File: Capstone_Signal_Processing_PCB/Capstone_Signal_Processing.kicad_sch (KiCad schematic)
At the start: 21 parts, among them J1 Conn_01x01, J2 Conn_01x01, J3 Conn_01x01, J4 Conn_01x04, J5 Conn_01x02, U1 AD4170-4BCPZ

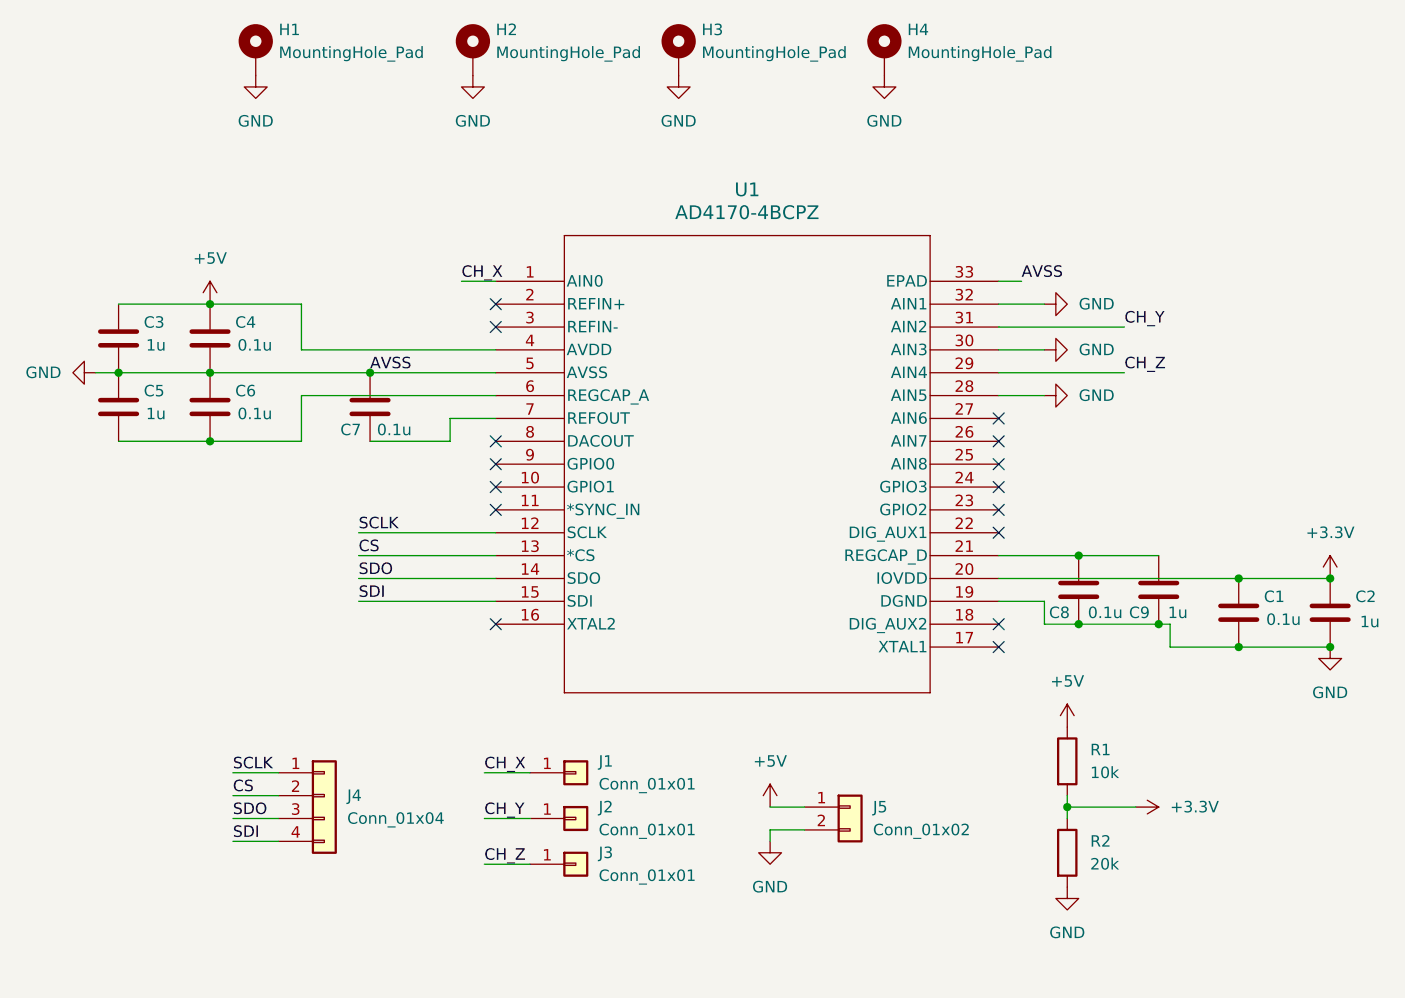
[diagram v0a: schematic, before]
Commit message: Fixes to Signal Processing PCB, Tx-Rx Added
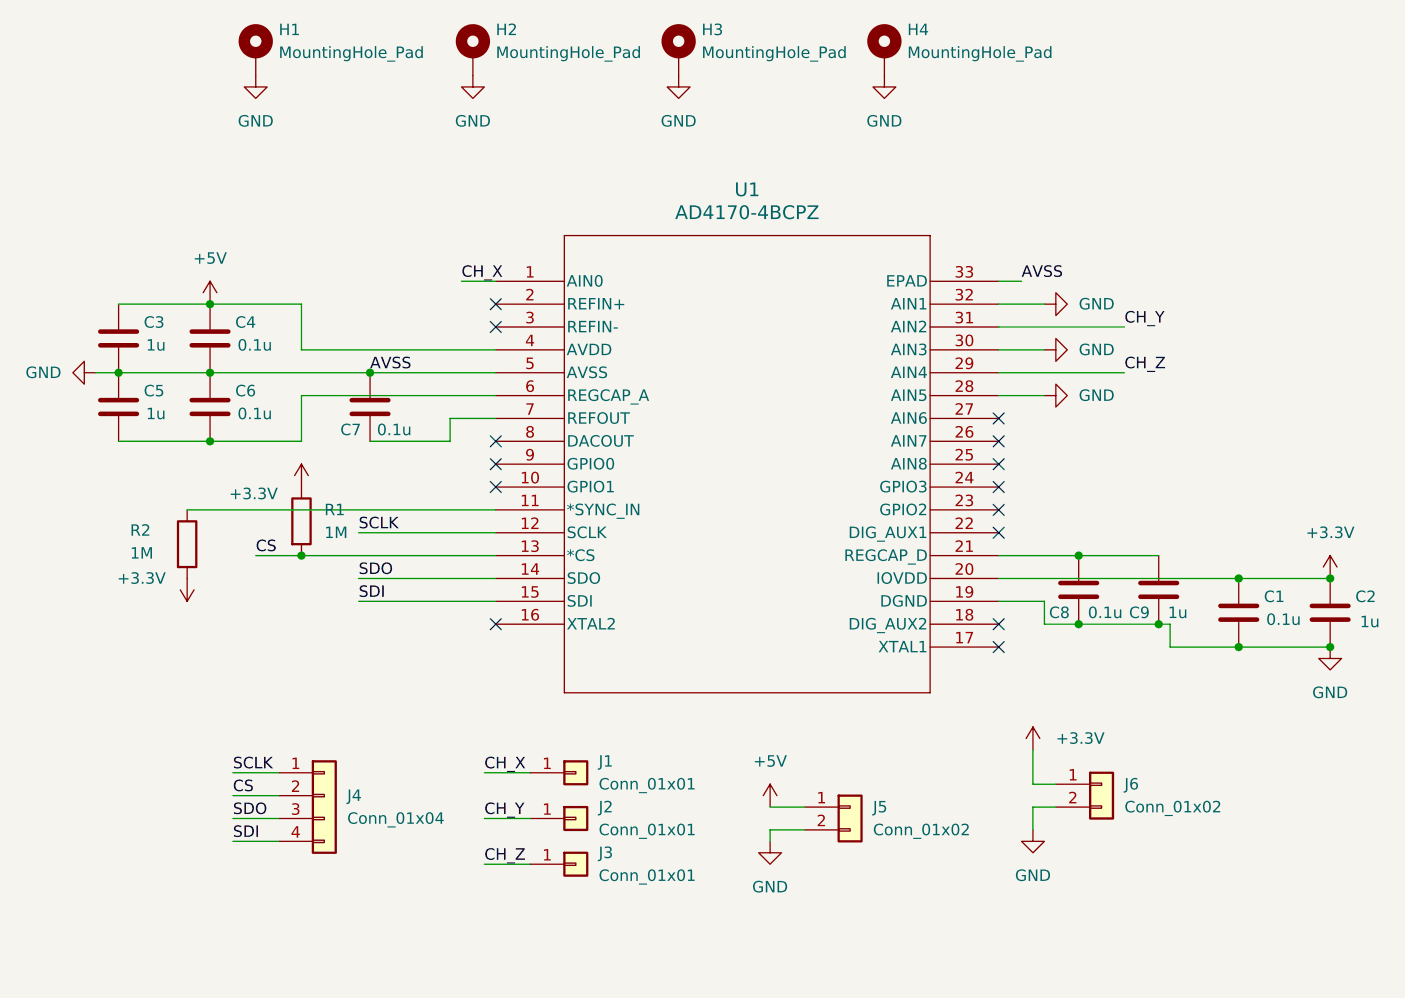
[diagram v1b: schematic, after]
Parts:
- added J6: Conn_01x02, Connector_JST:JST_XH_B2B-XH-AM_1x02_P2.50mm_Vertical, symbol Connector_Generic:Conn_01x02
- R1: value 10k -> 1M
- R2: value 20k -> 1M
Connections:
- net +3.3V: now also R1.1, R2.2, J6.1 (Pin_1); no longer R1.2, R2.1
- net +5V: no longer R1.1
- net CS: now also R1.2
- net GND: now also J6.2 (Pin_2); no longer R2.2
- net at U1.11 (*SYNC_IN): now also R2.1
- no-connect marks 15 -> 14

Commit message: Final Changes to ADC PCB
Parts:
- removed J1, J2, J3: Conn_01x01, Connector_JST:JST_XH_B1B-XH-AM_1x01_P2.50mm_Vertical, symbol Connector_Generic:Conn_01x01
- added J1, J2, J3, J7: Conn_01x02, Connector_JST:JST_XH_B2B-XH-AM_1x02_P2.50mm_Vertical, symbol Connector_Generic:Conn_01x02
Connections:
- net CH_X: now also J1.1 (Pin_1)
- net CH_Y: now also J2.1 (Pin_1)
- net CH_Z: now also J3.1 (Pin_1)
- net GND: no longer U1.28 (AIN5), U1.30 (AIN3), U1.32 (AIN1)
- net Ref+: now reaches U1.2 (REFIN+)
- net Ref+: now also J7.1 (Pin_1)
- net Ref-(GND): now reaches U1.3 (REFIN-)
- net Ref-(GND): now also J7.2 (Pin_2)
- new net CH_X_GND: J1.2 (Pin_2), U1.32 (AIN1)
- new net CH_Y_GND: J2.2 (Pin_2), U1.30 (AIN3)
- new net CH_Z_GND: J3.2 (Pin_2), U1.28 (AIN5)
- no-connect marks 14 -> 12
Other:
- moved on the sheet: J4
